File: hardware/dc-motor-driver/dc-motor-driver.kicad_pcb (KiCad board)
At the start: 2 copper layers, 94 x 100 mm, 125 parts, among them J10 OQ0232510000G, J11 OQ0232510000G, J12 OQ0232510000G, J13 OQ0232510000G, J15 OQ0232510000G, J16 OQ0232510000G, J17 OQ0232510000G, J18 OQ0232510000G, J19 OQ0232510000G, J2 VIN, J20 OQ0232510000G, J3 DE9, J4 Conn_01x02, Q1 2N7002, Q2 2N7002, Q3 Si2371EDS, Q4 Si2371EDS, U1 DRV8874PWPR, U2 DRV8874PWPR, U3 DRV8874PWPR, U4 DRV8874PWPR, U5 DRV8874PWPR, U6 DRV8874PWPR, U7 SP3485CN, U8 SP3485CN

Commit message: Added art to silkscreen
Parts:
- added G***: LOGO, LOGO, F.Cu at (165.8, 83.0)
- moved G*** 20.9 mm to (149.0, 96.5)
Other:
- board text added: "DEBUG CAN"
- board text removed: "M8 CAN"

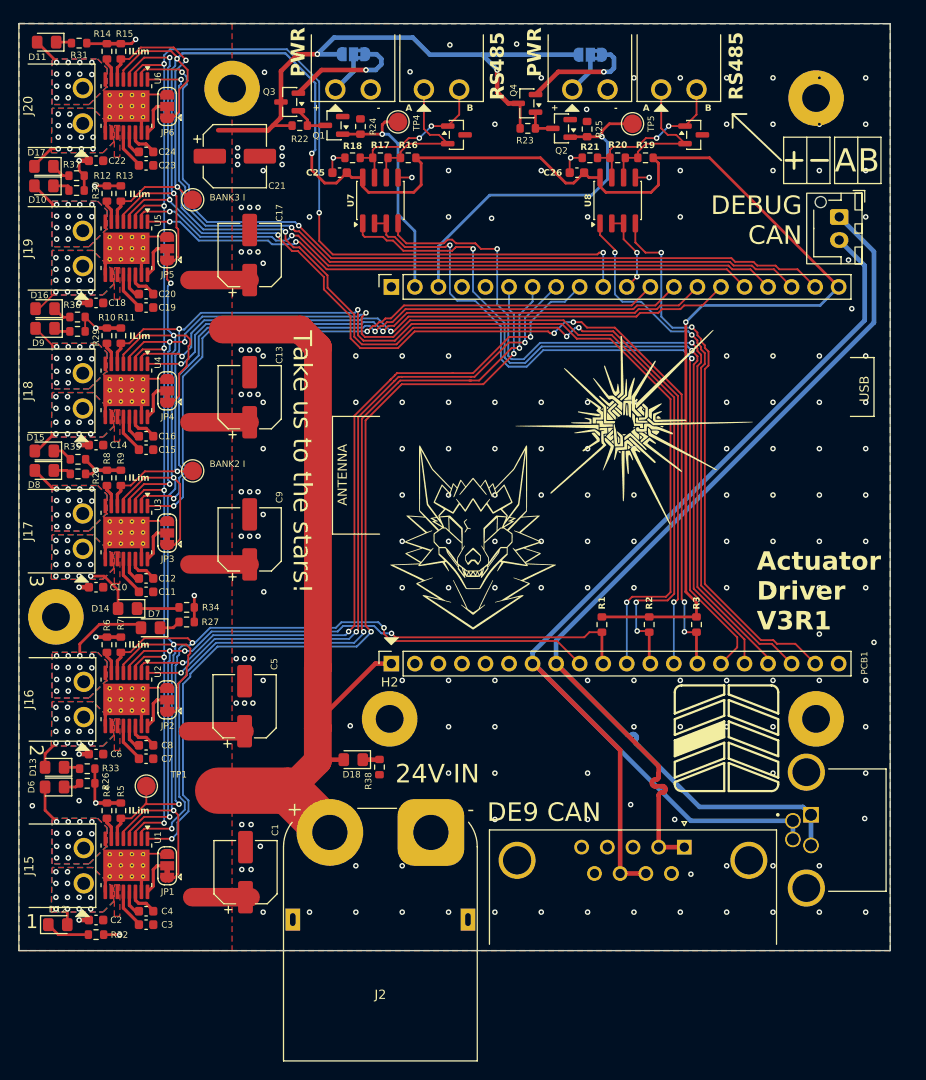
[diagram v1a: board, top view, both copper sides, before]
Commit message: Prod ready, fixed silkscreen and chamfered, plus readjusted stat LED placement
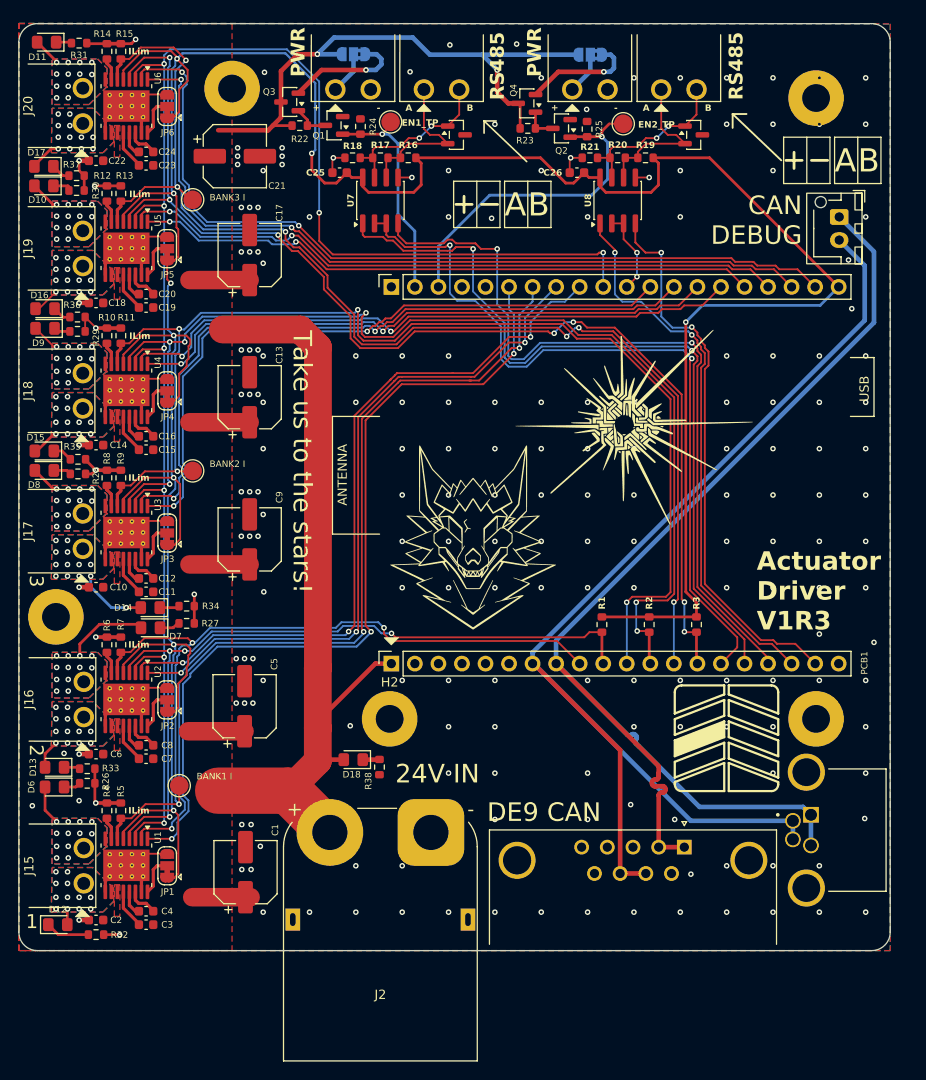
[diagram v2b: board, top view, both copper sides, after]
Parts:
- moved TP1 3.55 mm to (117.3, 122.2)
- moved D14 2.45 mm to (114.2, 103.0)
- moved TP5 1.00 mm to (165.2, 50.8)
- moved TP4 0.80 mm to (140.1, 50.6)
- moved R27 0.15 mm to (118.1, 104.7)
- moved R34 0.14 mm to (118.1, 102.8)
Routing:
- net Net-(D14-K): track 4.58 -> 2.26 mm
- net Net-(D14-A): track 5.17 -> 7.48 mm, vias 12 -> 13
- net /ENC_PWR_SW_1: track 25.6 -> 24.5 mm
- net /ENC_PWR_SW_2: track 38.1 -> 37.1 mm
- net GND: vias 203 -> 201
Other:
- outline, holes or cut-outs redrawn
- board text added: "Actuator Driver V1R3"
- board text added: "BANK1 I"
- board text added: "CAN DEBUG"
- board text added: "EN1_TP"
- board text added: "EN2_TP"
- board text removed: "Actuator Driver V3R1"
- board text removed: "DEBUG CAN"
